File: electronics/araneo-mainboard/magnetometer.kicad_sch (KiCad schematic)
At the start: 7 parts, among them IC2 BMI270

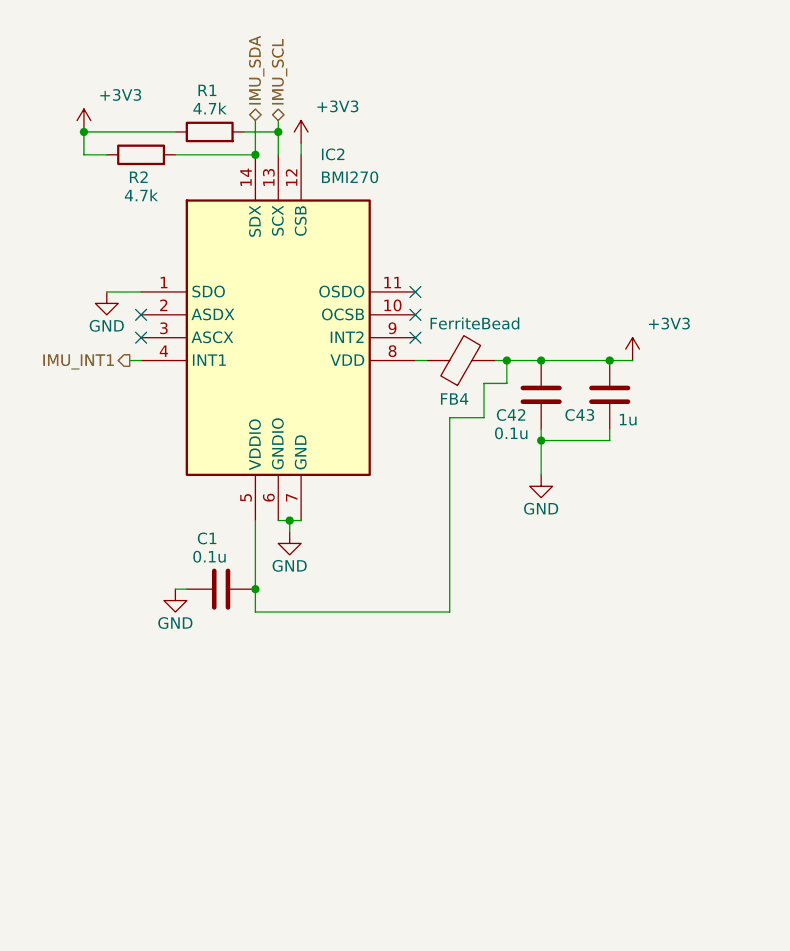
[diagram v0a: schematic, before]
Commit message: electronics: add magnetometer
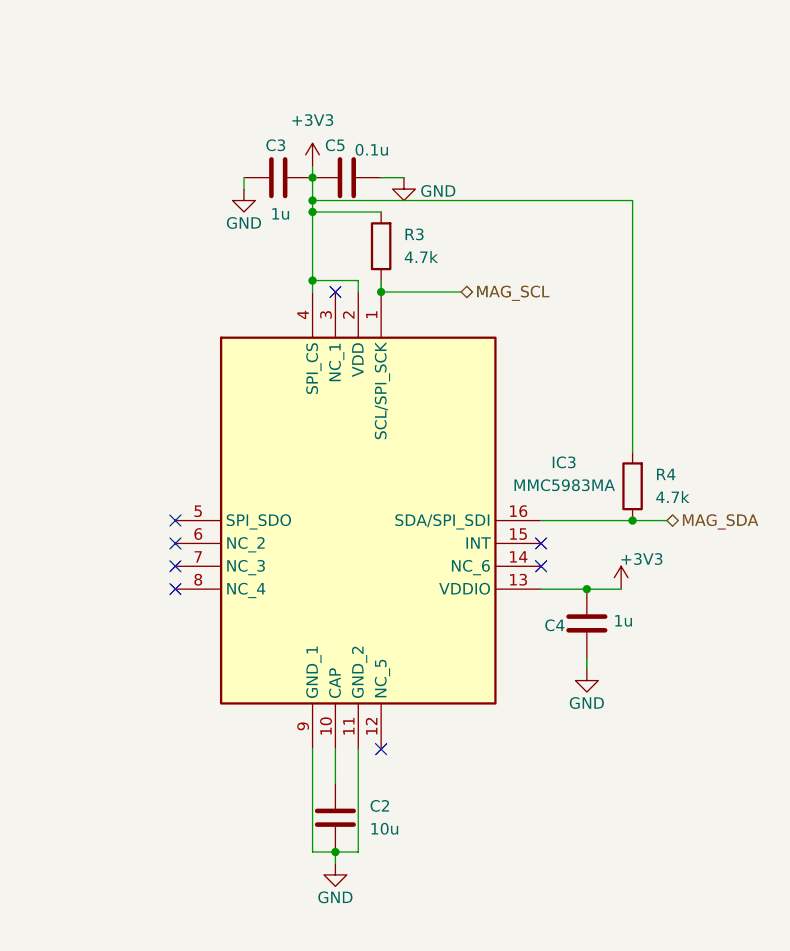
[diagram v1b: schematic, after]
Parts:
- removed C1, C42: 0.1u, Capacitor_SMD:C_0603_1608Metric_Pad1.08x0.95mm_HandSolder, symbol Device:C
- removed C43: 1u, Capacitor_SMD:C_0603_1608Metric_Pad1.08x0.95mm_HandSolder, symbol Device:C
- removed FB4: FerriteBead, Resistor_SMD:R_0603_1608Metric_Pad0.98x0.95mm_HandSolder, symbol Device:FerriteBead
- removed IC2: BMI270, custom_footprints:BMI270, symbol Symbols:BMI270
- removed R1, R2: 4.7k, Resistor_SMD:R_0603_1608Metric_Pad0.98x0.95mm_HandSolder, symbol Device:R
- added C2: 10u, Capacitor_SMD:C_1206_3216Metric_Pad1.33x1.80mm_HandSolder, symbol Device:C
- added C3, C4: 1u, Capacitor_SMD:C_0603_1608Metric_Pad1.08x0.95mm_HandSolder, symbol Device:C
- added C5: 0.1u, Capacitor_SMD:C_0603_1608Metric_Pad1.08x0.95mm_HandSolder, symbol Device:C
- added IC3: MMC5983MA, custom_footprints:MMC5983MA, symbol Symbols:MMC5983MA
- added R3, R4: 4.7k, Resistor_SMD:R_0603_1608Metric_Pad0.98x0.95mm_HandSolder, symbol Device:R
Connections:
- net +3V3: now also C3.2, C4.2, C5.2, IC3.13 (VDDIO), IC3.2 (VDD), IC3.4 (SPI_CS), R3.2, R4.2
- net GND: now also C2.2, C3.1, C4.1, C5.1, IC3.11 (GND_2), IC3.9 (GND_1)
- new net: C2.1, IC3.10 (CAP)
- new net MAG_SCL: IC3.1 (SCL/SPI_SCK), R3.1
- new net MAG_SDA: IC3.16 (SDA/SPI_SDI), R4.1
- no-connect marks 5 -> 8

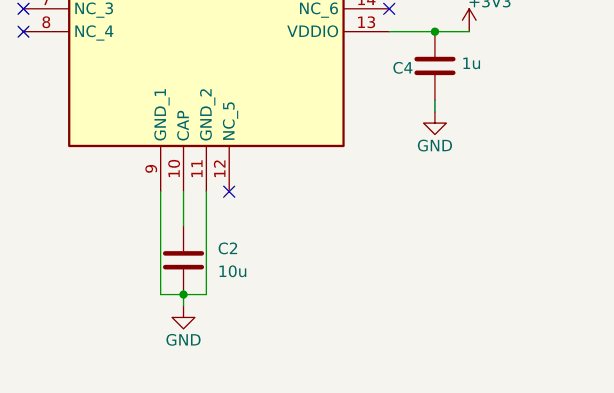
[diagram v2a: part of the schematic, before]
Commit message: electronics: remove unnecessary capacitors, add net labels, change screw terminal to JST_XH
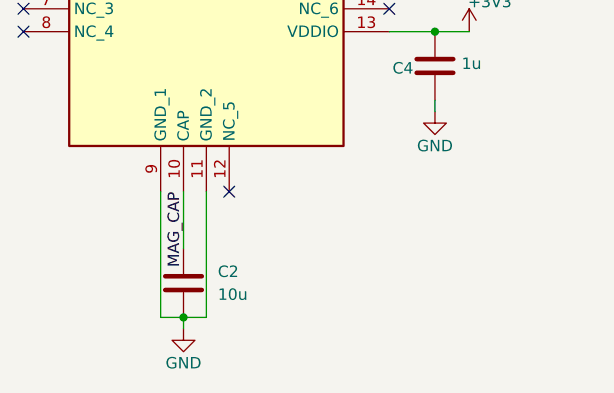
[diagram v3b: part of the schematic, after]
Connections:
- net MAG_CAP: now reaches C2.1, IC3.10 (CAP)
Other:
- moved on the sheet: C2
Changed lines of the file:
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@@
 	(paper "A4")
+	(junction
+		(at 71.12 105.41)
+		(diameter 0)
+		(color 0 0 0 0)
+	)
 	(junction
 		(at 68.58 30.48)
@@
 	)
 	(junction
-		(at 71.12 102.87)
-		(diameter 0)
-		(color 0 0 0 0)
-	)
-	(junction
 		(at 68.58 39.37)
 		(diameter 0)
@@
 	(wire
 		(pts
-			(xy 68.58 102.87) (xy 71.12 102.87)
+			(xy 68.58 105.41) (xy 71.12 105.41)
 		)
 		(stroke
@@
 	(wire
 		(pts
-			(xy 68.58 91.44) (xy 68.58 102.87)
-		)
-		(stroke
-			(width 0)
-			(type default)
-		)
-	)
-	(wire
-		(pts
-			(xy 73.66 91.44) (xy 73.66 102.87)
-		)
-		(stroke
-			(width 0)
-			(type default)
-		)
-	)
-	(wire
-		(pts
-			(xy 73.66 102.87) (xy 71.12 102.87)
+			(xy 68.58 91.44) (xy 68.58 105.41)
+		)
+		(stroke
+			(width 0)
+			(type default)
+		)
+	)
+	(wire
+		(pts
+			(xy 73.66 91.44) (xy 73.66 105.41)
+		)
+		(stroke
+			(width 0)
+			(type default)
+		)
+	)
+	(wire
+		(pts
+			(xy 73.66 105.41) (xy 71.12 105.41)
 		)
 		(stroke
@@
 	(wire
 		(pts
-			(xy 71.12 91.44) (xy 71.12 95.25)
+			(xy 71.12 91.44) (xy 71.12 97.79)
 		)
 		(stroke
@@
 	(wire
 		(pts
-			(xy 71.12 102.87) (xy 71.12 104.14)
-		)
-		(stroke
-			(width 0)
-			(type default)
-		)
-	)
-	(wire
-		(pts
 			(xy 93.98 66.04) (xy 104.14 66.04)
 		)
@@
 			(width 0)
 			(type default)
+		)
+	)
+	(wire
+		(pts
+			(xy 71.12 105.41) (xy 71.12 106.68)
+		)
+		(stroke
+			(width 0)
+			(type default)
+		)
+	)
+	(label "MAG_CAP"
+		(at 71.12 91.44 270)
+		(effects
+			(font
+				(size 1.27 1.27)
+			)
+			(justify right bottom)
 		)
 	)
@@
 	(symbol
 		(lib_id "Device:C")
-		(at 71.12 99.06 0)
+		(at 71.12 101.6 0)
 		(unit 1)
 		(body_style 1)
@@
 		(fields_autoplaced yes)
 		(property "Reference" "C2"
-			(at 74.93 97.7899 0)
+			(at 74.93 100.3299 0)
 			(show_name no)
 			(do_not_autoplace no)
@@
 		)
 		(property "Value" "10u"
-			(at 74.93 100.3299 0)
+			(at 74.93 102.8699 0)
 			(show_name no)
 			(do_not_autoplace no)
@@
 		)
 		(property "Footprint" "Capacitor_SMD:C_1206_3216Metric_Pad1.33x1.80mm_HandSolder"
-			(at 72.0852 102.87 0)
+			(at 72.0852 105.41 0)
 			(hide yes)
 			(show_name no)
@@
 		)
 		(property "Datasheet" ""
-			(at 71.12 99.06 0)
+			(at 71.12 101.6 0)
 			(hide yes)
 			(show_name no)
@@
 		)
 		(property "Description" "Unpolarized capacitor"
-			(at 71.12 99.06 0)
+			(at 71.12 101.6 0)
 			(hide yes)
 			(show_name no)
@@
 	(symbol
 		(lib_id "PCM_SparkFun-PowerSymbol:GND")
-		(at 71.12 104.14 0)
+		(at 71.12 106.68 0)
 		(unit 1)
 		(body_style 1)
@@
 		(fields_autoplaced yes)
 		(property "Reference" "#PWR081"
+			(at 71.12 113.03 0)
+			(hide yes)
+			(show_name no)
+			(do_not_autoplace no)
+			(effects
+				(font
+					(size 1.27 1.27)
+				)
+			)
+		)
+		(property "Value" "GND"
 			(at 71.12 110.49 0)
-			(hide yes)
-			(show_name no)
-			(do_not_autoplace no)
-			(effects
-				(font
-					(size 1.27 1.27)
-				)
-			)
-		)
-		(property "Value" "GND"
-			(at 71.12 107.95 0)
 			(show_name no)
 			(do_not_autoplace yes)
@@
 		)
 		(property "Footprint" ""
-			(at 71.12 104.14 0)
+			(at 71.12 106.68 0)
 			(hide yes)
 			(show_name no)
@@
 		)
 		(property "Datasheet" ""
-			(at 71.12 104.14 0)
+			(at 71.12 106.68 0)
 			(hide yes)
 			(show_name no)
@@
 		)
 		(property "Description" "Power symbol creates a global label with name \"GND\" , ground"
-			(at 71.12 113.03 0)
-			(hide yes)
-			(show_name no)
+			(at 71.12 115.57 0)
+			(hide yes)
+			(show_name no)
